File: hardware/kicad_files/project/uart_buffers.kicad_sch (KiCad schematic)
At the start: 4 parts, among them J5 Conn_01x02_Pin, U10 SN74LVC1G125DCKR, U9 SN74LVC1G125DCKR

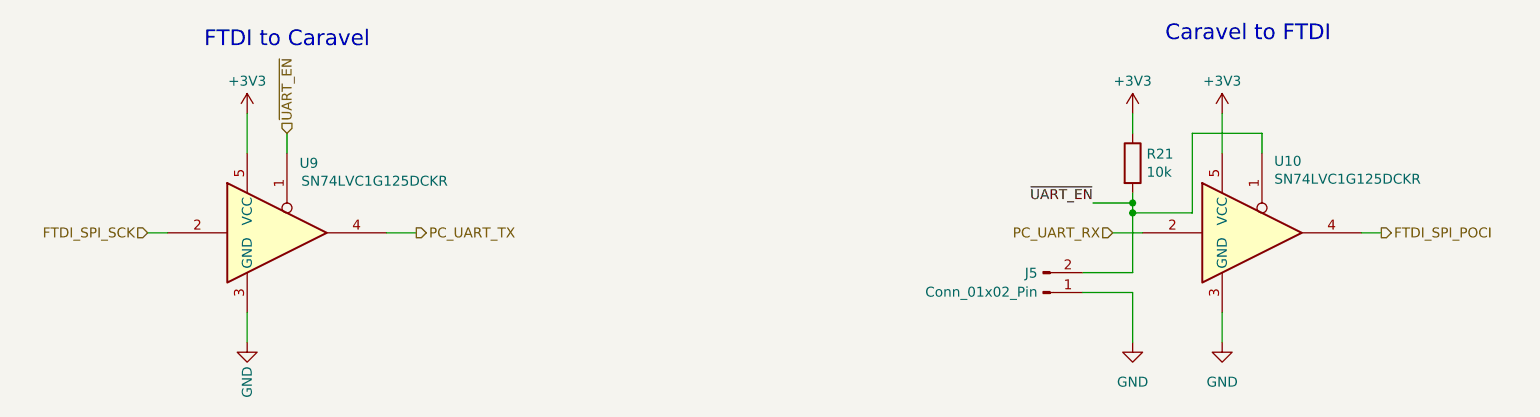
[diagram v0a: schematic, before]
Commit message: feat: update to 0.2
feat: add pin sockets compatible to the Pmod interface

feat: add a power switch and an overcurrent protection circuit, including a fault status LED and a solder bridge

fix: remove the clock jumpers and directly connect the second output clock to the user clock input

misc: remove the jumpers from io 36 and 37 to the bitbang inputs, add bitbang pins to the UART connector

cosmetic: make the PCB edges round
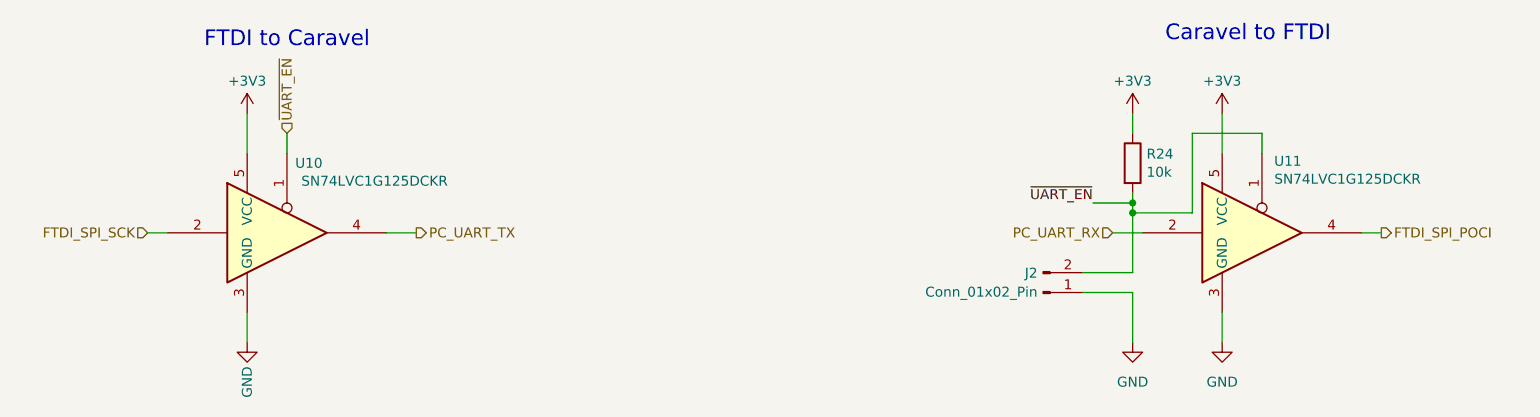
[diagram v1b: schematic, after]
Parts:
- renumbered J5 to J2, R21 to R24, U9 to U10, U10 to U11
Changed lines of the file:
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@@
 		(title "UART Buffers")
 		(date "2024-05-30")
-		(rev "0.1.1")
+		(rev "0.2.0")
 	)
 	(junction
@@
 		(on_board yes)
 		(dnp no)
-		(property "Reference" "#PWR069"
+		(property "Reference" "#PWR76"
 			(at 87.63 116.84 0)
 			(effects
@@
 			(project "FABulous_board"
 				(path "/5664f05e-a3ef-4177-8026-c4580fa32c71/4820c043-623b-447e-8e47-990cd78f4dc2"
-					(reference "#PWR069")
+					(reference "#PWR76")
 					(unit 1)
 				)
@@
 		(dnp no)
 		(fields_autoplaced yes)
-		(property "Reference" "#PWR070"
+		(property "Reference" "#PWR77"
 			(at 200.66 85.09 0)
 			(effects
@@
 			(project "FABulous_board"
 				(path "/5664f05e-a3ef-4177-8026-c4580fa32c71/4820c043-623b-447e-8e47-990cd78f4dc2"
-					(reference "#PWR070")
+					(reference "#PWR77")
 					(unit 1)
 				)
@@
 		(dnp no)
 		(fields_autoplaced yes)
-		(property "Reference" "#PWR068"
+		(property "Reference" "#PWR75"
 			(at 87.63 85.09 0)
 			(effects
@@
 			(project "FABulous_board"
 				(path "/5664f05e-a3ef-4177-8026-c4580fa32c71/4820c043-623b-447e-8e47-990cd78f4dc2"
-					(reference "#PWR068")
+					(reference "#PWR75")
 					(unit 1)
 				)
@@
 		(on_board yes)
 		(dnp no)
-		(property "Reference" "#PWR073"
+		(property "Reference" "#PWR80"
 			(at 212.09 116.84 0)
 			(effects
@@
 			(project "FABulous_board"
 				(path "/5664f05e-a3ef-4177-8026-c4580fa32c71/4820c043-623b-447e-8e47-990cd78f4dc2"
-					(reference "#PWR073")
+					(reference "#PWR80")
 					(unit 1)
 				)
@@
 		(on_board yes)
 		(dnp no)
-		(property "Reference" "R21"
+		(property "Reference" "R24"
 			(at 202.438 86.4616 0)
 			(effects
@@
 			(project "FABulous_board"
 				(path "/5664f05e-a3ef-4177-8026-c4580fa32c71/4820c043-623b-447e-8e47-990cd78f4dc2"
-					(reference "R21")
+					(reference "R24")
 					(unit 1)
 				)
@@
 		(on_board yes)
 		(dnp no)
-		(property "Reference" "#PWR071"
+		(property "Reference" "#PWR78"
 			(at 200.66 116.84 0)
 			(effects
@@
 			(project "FABulous_board"
 				(path "/5664f05e-a3ef-4177-8026-c4580fa32c71/4820c043-623b-447e-8e47-990cd78f4dc2"
-					(reference "#PWR071")
+					(reference "#PWR78")
 					(unit 1)
 				)
@@
 		(dnp no)
 		(fields_autoplaced yes)
-		(property "Reference" "J5"
+		(property "Reference" "J2"
 			(at 188.5189 101.6578 0)
 			(effects
@@
 			(project ""
 				(path "/5664f05e-a3ef-4177-8026-c4580fa32c71/4820c043-623b-447e-8e47-990cd78f4dc2"
-					(reference "J5")
+					(reference "J2")
 					(unit 1)
 				)
@@
 		(on_board yes)
 		(dnp no)
-		(property "Reference" "U10"
+		(property "Reference" "U11"
 			(at 220.472 87.376 0)
 			(effects
@@
 		(property "Field7" "1470771"
 			(at 217.17 96.52 0)
+			(effects
+				(font
+					(size 1.27 1.27)
+				)
+				(justify left bottom)
+				(hide yes)
+			)
+		)
+		(pin "1"
+		)
+		(pin "2"
+		)
+		(pin "3"
+		)
+		(pin "4"
+		)
+		(pin "5"
+		)
+		(instances
+			(project "FABulous_board"
+				(path "/5664f05e-a3ef-4177-8026-c4580fa32c71/4820c043-623b-447e-8e47-990cd78f4dc2"
+					(reference "U11")
+					(unit 1)
+				)
+			)
+		)
+	)
+	(symbol
+		(lib_id "74xGxx:SN74LVC1G125DCK")
+		(at 92.71 96.52 0)
+		(unit 1)
+		(exclude_from_sim no)
+		(in_bom yes)
+		(on_board yes)
+		(dnp no)
+		(property "Reference" "U10"
+			(at 95.504 87.63 0)
+			(effects
+				(font
+					(size 1.27 1.27)
+				)
+			)
+		)
+		(property "Value" "SN74LVC1G125DCKR"
+			(at 103.886 89.916 0)
+			(effects
+				(font
+					(size 1.27 1.27)
+				)
+			)
+		)
+		(property "Footprint" "Package_TO_SOT_SMD:Texas_R-PDSO-G5_DCK-5"
+			(at 92.71 96.52 0)
+			(effects
+				(font
+					(size 1.27 1.27)
+				)
+				(hide yes)
+			)
+		)
+		(property "Datasheet" "http://www.ti.com/lit/ds/symlink/sn74lvc1g125.pdf"
+			(at 92.71 96.52 0)
+			(effects
+				(font
+					(size 1.27 1.27)
+				)
+				(hide yes)
+			)
+		)
+		(property "Description" "Single Buffer Gate Tri-State, Low-Voltage CMOS, SOT-353"
+			(at 92.71 96.52 0)
+			(effects
+				(font
+					(size 1.27 1.27)
+				)
+				(hide yes)
+			)
+		)
+		(property "Field4" "76C4082"
+			(at 92.71 96.52 0)
+			(effects
+				(font
+					(size 1.27 1.27)
+				)
+				(justify left bottom)
+				(hide yes)
+			)
+		)
+		(property "Field5" "Texas Instruments"
+			(at 92.71 96.52 0)
+			(effects
+				(font
+					(size 1.27 1.27)
+				)
+				(justify left bottom)
+				(hide yes)
+			)
+		)
+		(property "Field6" "SN74LVC1G125DCKR"
+			(at 92.71 96.52 0)
+			(effects
+				(font
+					(size 1.27 1.27)
+				)
+				(justify left bottom)
+				(hide yes)
+			)
+		)
+		(property "Field7" "1470771"
+			(at 92.71 96.52 0)
 			(effects
 				(font
@@
 	)
 	(symbol
-		(lib_id "74xGxx:SN74LVC1G125DCK")
-		(at 92.71 96.52 0)
-		(unit 1)
-		(exclude_from_sim no)
-		(in_bom yes)
-		(on_board yes)
-		(dnp no)
-		(property "Reference" "U9"
-			(at 95.504 87.63 0)
-			(effects
-				(font
-					(size 1.27 1.27)
-				)
-			)
-		)
-		(property "Value" "SN74LVC1G125DCKR"
-			(at 103.886 89.916 0)
-			(effects
-				(font
-					(size 1.27 1.27)
-				)
-			)
-		)
-		(property "Footprint" "Package_TO_SOT_SMD:Texas_R-PDSO-G5_DCK-5"
-			(at 92.71 96.52 0)
-			(effects
-				(font
-					(size 1.27 1.27)
-				)
-				(hide yes)
-			)
-		)
-		(property "Datasheet" "http://www.ti.com/lit/ds/symlink/sn74lvc1g125.pdf"
-			(at 92.71 96.52 0)
-			(effects
-				(font
-					(size 1.27 1.27)
-				)
-				(hide yes)
-			)
-		)
-		(property "Description" "Single Buffer Gate Tri-State, Low-Voltage CMOS, SOT-353"
-			(at 92.71 96.52 0)
-			(effects
-				(font
-					(size 1.27 1.27)
-				)
-				(hide yes)
-			)
-		)
-		(property "Field4" "76C4082"
-			(at 92.71 96.52 0)
-			(effects
-				(font
-					(size 1.27 1.27)
-				)
-				(justify left bottom)
-				(hide yes)
-			)
-		)
-		(property "Field5" "Texas Instruments"
-			(at 92.71 96.52 0)
-			(effects
-				(font
-					(size 1.27 1.27)
-				)
-				(justify left bottom)
-				(hide yes)
-			)
-		)
-		(property "Field6" "SN74LVC1G125DCKR"
-			(at 92.71 96.52 0)
-			(effects
-				(font
-					(size 1.27 1.27)
-				)
-				(justify left bottom)
-				(hide yes)
-			)
-		)
-		(property "Field7" "1470771"
-			(at 92.71 96.52 0)
-			(effects
-				(font
-					(size 1.27 1.27)
-				)
-				(justify left bottom)
-				(hide yes)
-			)
-		)
-		(pin "1"
-		)
-		(pin "2"
-		)
-		(pin "3"
-		)
-		(pin "4"
-		)
-		(pin "5"
-		)
-		(instances
-			(project "FABulous_board"
-				(path "/5664f05e-a3ef-4177-8026-c4580fa32c71/4820c043-623b-447e-8e47-990cd78f4dc2"
-					(reference "U9")
-					(unit 1)
-				)
-			)
-		)
-	)
-	(symbol
 		(lib_id "power:+3V3")
 		(at 212.09 81.28 0)
@@
 		(dnp no)
 		(fields_autoplaced yes)
-		(property "Reference" "#PWR072"
+		(property "Reference" "#PWR79"
 			(at 212.09 85.09 0)
 			(effects
@@
 			(project "FABulous_board"
 				(path "/5664f05e-a3ef-4177-8026-c4580fa32c71/4820c043-623b-447e-8e47-990cd78f4dc2"
-					(reference "#PWR072")
+					(reference "#PWR79")
 					(unit 1)
 				)
